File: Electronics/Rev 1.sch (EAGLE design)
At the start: 90 parts, among them Q1 BCV27, Q10 BCV26SOT23, Q11 BCV27, Q12 BCV26SOT23, Q13 BCV27, Q14 BCV26SOT23, Q15 BCV27, Q16 BCV26SOT23, Q17 BCV27, Q18 BCV26SOT23, Q19 BCV27, Q2 BCV26SOT23, Q20 BCV26SOT23, Q21 BCV27, Q22 BCV26SOT23, Q23 BCV27, Q24 BCV26SOT23, Q25 PBSS4360XFPBSS4360XF, Q26 MMBT3904,215MMBT3904,215, Q27 PBSS4360XFPBSS4360XF, Q28 MMBT3904,215MMBT3904,215, Q29 PBSS4360XFPBSS4360XF, Q3 BCV27, Q30 TIP35CTIP35C, Q31 PBSS4360XFPBSS4360XF, Q32 MMBT3904,215MMBT3904,215, Q33 TIP35CTIP35C, Q34 PBSS4360XFPBSS4360XF, Q35 MMBT3904,215MMBT3904,215, Q4 BCV26SOT23, Q5 BCV27, Q6 BCV26SOT23, Q7 BCV27, Q8 BCV26SOT23, Q9 BCV27, U1 LFXP6E-3FN256C, U2 MCP4251, U3 MCP4251, U4 MMA8453QR116QFN

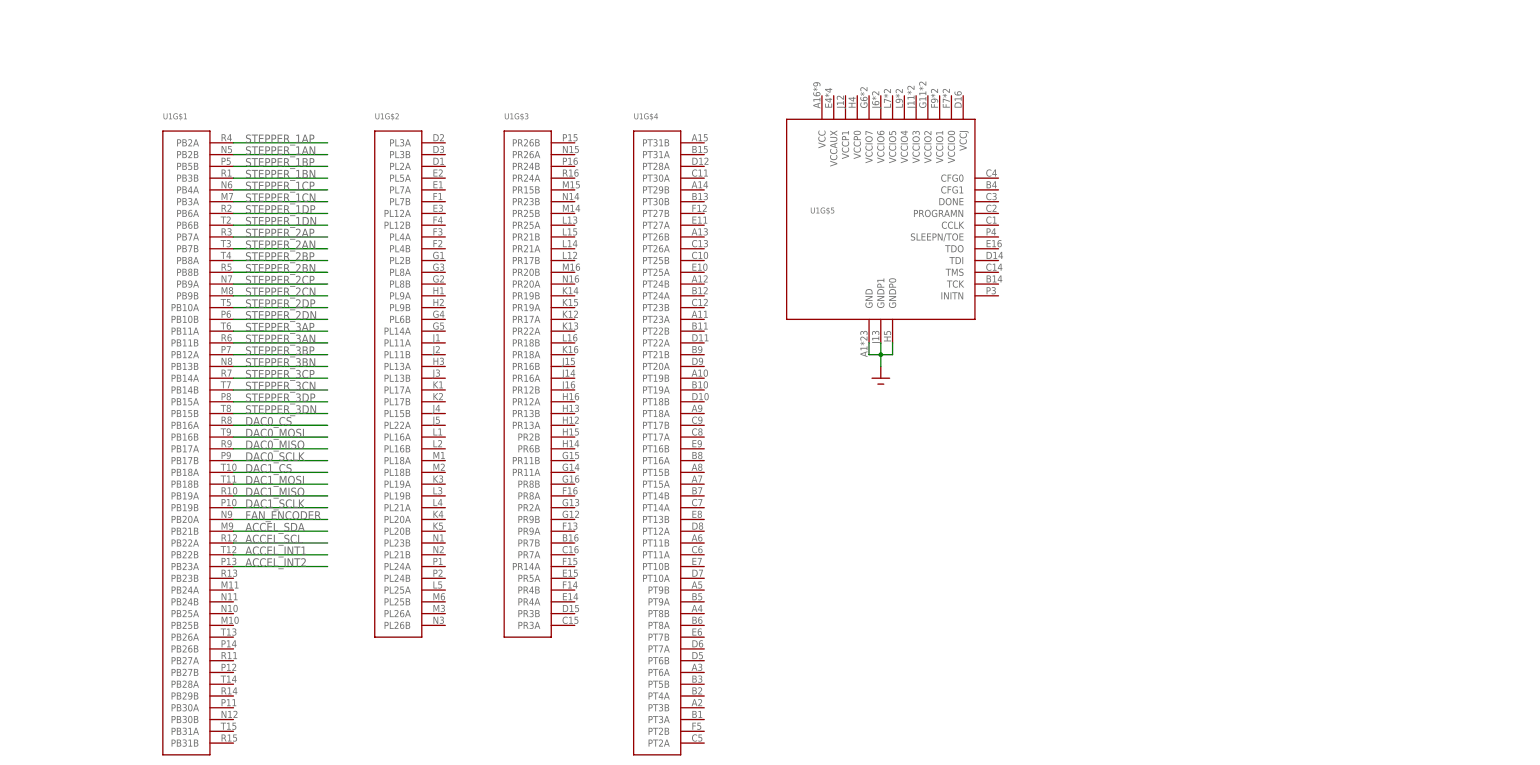
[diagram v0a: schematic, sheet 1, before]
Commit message: Did most of the rest of the schematic
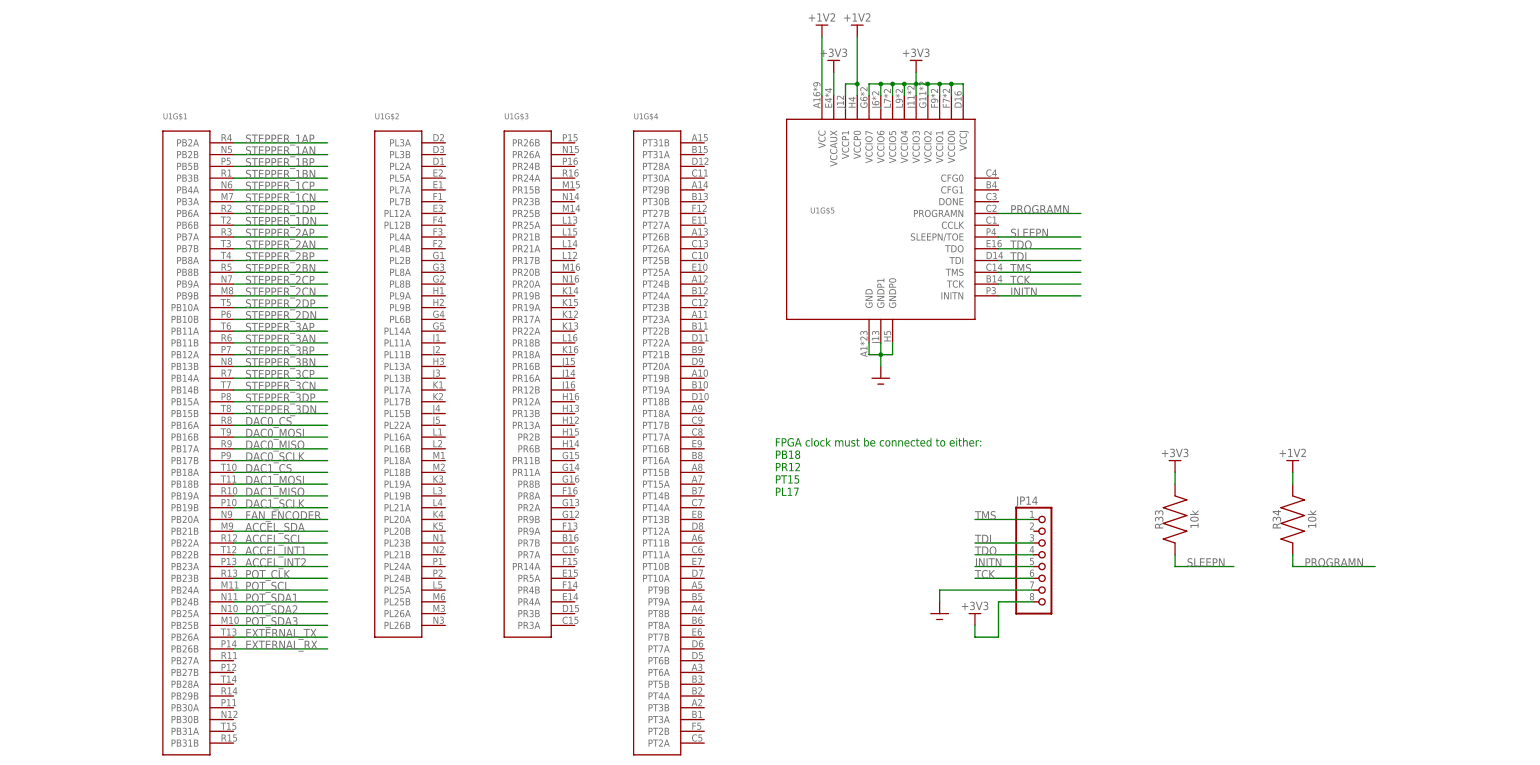
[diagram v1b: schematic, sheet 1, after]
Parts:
- added C27, C28, C29, C30, C31, C32: 0.1uF, fillament-winder:CAPACITOR0805
- added C33: 1uF, fillament-winder:CAPACITOR0805
- added JP11: (no value), fillament-winder:PINHD-1X6
- added JP12, JP13: (no value), fillament-winder:PINHD-1X7
- added JP14: (no value), fillament-winder:PINHD-1X8
- added Q36, Q37, Q38, Q39: MMBT3904,215MMBT3904,215, fillament-winder:MMBT3904,215MMBT3904,215
- added R16, R17, R18: POTENTIOMETER, fillament-winder:POTENTIOMETER
- added R19, R20, R21, R22, R25, R28, R33, R34: 10k, fillament-winder:RESISTOR0805
- added R23, R24, R27: 0R, fillament-winder:RESISTOR0805
- added R26: 1k, fillament-winder:RESISTOR0805
- added U10: RPI, fillament-winder:RPI
- added U5, U6, U7: 74AHC1G66GW,125TSSOP6, fillament-winder:74AHC1G66GW,125TSSOP6
- added U8: MCP3021A1T-E/OTSOT23, fillament-winder:MCP3021A1T-E/OTSOT23
- added U9: MC74HC164BDR2GMC74HC164BDR2G, fillament-winder:MC74HC164BDR2GMC74HC164BDR2G
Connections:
- new net +1V2: R34.P$2, U1G$5.VCC, U1G$5.VCCP0, U1G$5.VCCP1
- new net +5V: C33.P$2, U10.+5V
- new net EXTERNAL_RX: U10.RX, U1G$1.PB26B
- new net EXTERNAL_TX: U10.TX, U1G$1.PB26A
- new net INITN: JP14.5, U1G$5.INITN
- new net N$15: R16.P$1, U5.Y
- new net N$16: R17.P$1, U6.Y
- new net N$19: R18.P$1, U7.Y
- new net N$20: Q36.B, R21.P$2
- new net N$21: R19.P$1, U9.A1
- new net N$22: Q37.B, R22.P$2
- new net N$23: R23.P$1, R24.P$1, U9.QC
- new net N$24: Q38.B, R25.P$2
- new net N$25: Q39.B, R26.P$2
- new net N$27: Q39.E, R27.P$1
- new net POT_ADC: U5.Z, U6.Z, U7.Z, U8.AIN
- new net POT_CLK: JP11.3, JP12.3, JP13.3, U1G$1.PB23B, U9.CLK
- new net POT_RST: R24.P$2, U9.QD, U9.RST
- new net POT_SCL: JP11.4, JP12.4, JP13.4, U1G$1.PB24A, U8.SCL
- new net POT_SDA1: JP12.5, JP13.5, U1G$1.PB24B, U8.SDA
- new net POT_SDA2: JP11.5, JP12.6, JP13.6, U1G$1.PB25A
- new net POT_SDA3: JP11.6, JP12.7, JP13.7, U1G$1.PB25B
- new net POT_SEL_1: R23.P$2, R25.P$1, R27.P$2, U5.E
- new net POT_SEL_2: R21.P$1, R28.P$1, U6.E, U9.QA
- new net POT_SEL_3: R22.P$1, U7.E, U9.QB
- new net POT_SEL_IN: R26.P$1
- new net POT_SHIFT_IN: Q36.C, Q37.C, Q38.C, R20.P$1, U9.A2
- new net PROGRAMN: R34.P$1, U1G$5.PROGRAMN
- new net SLEEPN: R33.P$1, U1G$5.SLEEPN/TOE
- new net TCK: JP14.6, U1G$5.TCK
- new net TDI: JP14.3, U1G$5.TDI
- new net TDO: JP14.4, U1G$5.TDO
- new net TMS: JP14.1, U1G$5.TMS
- net +3V3: now also C27.P$2, C28.P$2, C29.P$2, C30.P$2, C31.P$2, C32.P$2, JP11.1, JP12.1, JP13.1, JP14.8, Q39.C, R19.P$2, R20.P$2, R28.P$2, R33.P$2, U1G$5.VCCAUX, U1G$5.VCCIO0, U1G$5.VCCIO1, U1G$5.VCCIO2, U1G$5.VCCIO3, U1G$5.VCCIO4, U1G$5.VCCIO5, U1G$5.VCCIO6, U1G$5.VCCIO7, U1G$5.VCCJ, U5.VCC, U6.VCC, U7.VCC, U8.VDD, U9.VCC
- net GND: now also C27.P$1, C28.P$1, C29.P$1, C30.P$1, C31.P$1, C32.P$1, C33.P$1, JP11.2, JP12.2, JP13.2, JP14.7, Q36.E, Q37.E, Q38.E, U10.GND, U5.GND, U6.GND, U7.GND, U8.VSS, U9.GND
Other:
- note added: "FPGA clock must be connected to either: PB18 PR12 PT15 PL17"

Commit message: Finished more of the schematic
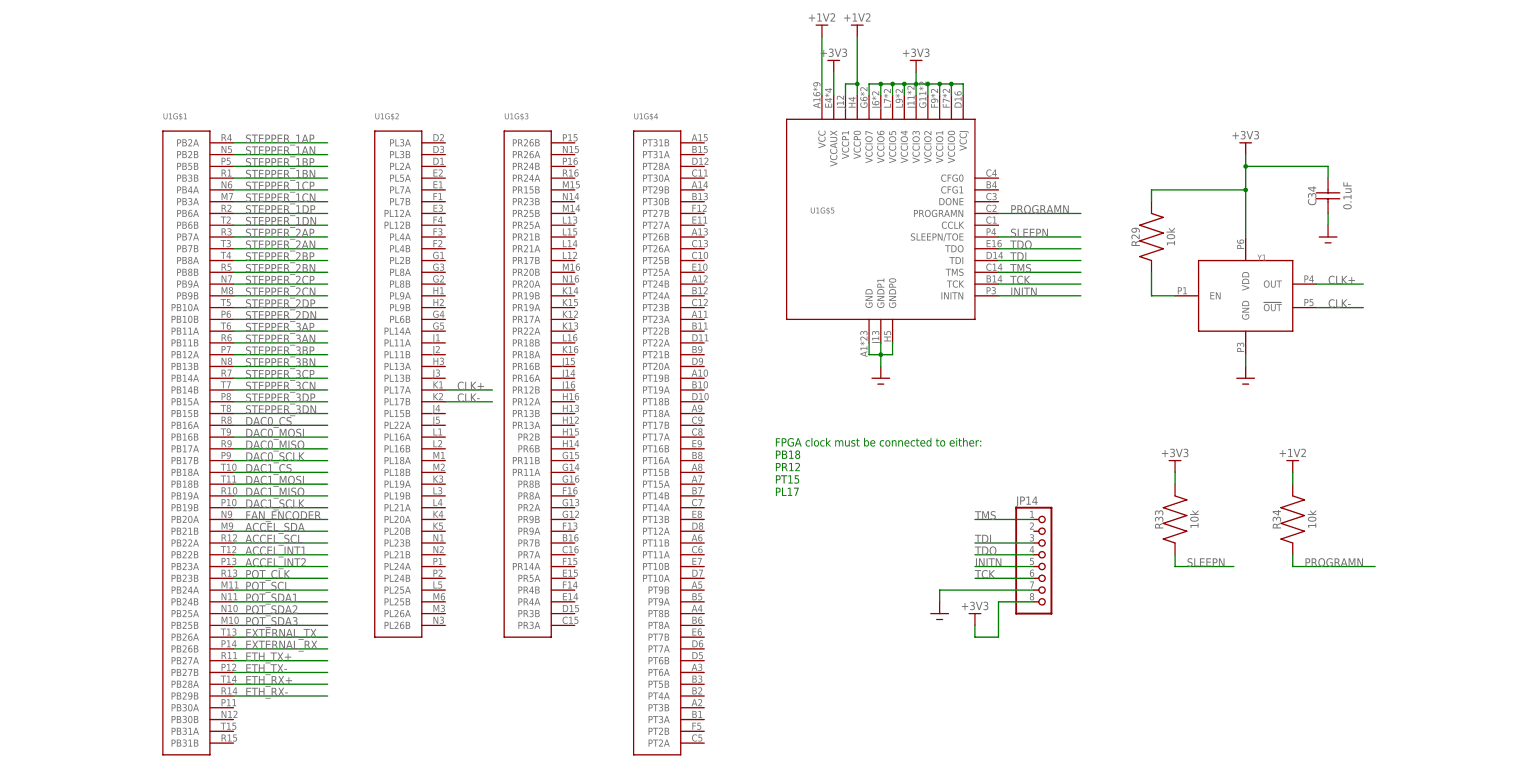
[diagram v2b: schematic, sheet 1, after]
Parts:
- added C34, C35, C36, C37, C38: 0.1uF, fillament-winder:CAPACITOR0805
- added P1: 5-2301994-4, fillament-winder:5-2301994-4
- added R29: 10k, fillament-winder:RESISTOR0805
- added R30, R31, R32, R35: 49.9R, fillament-winder:RESISTOR0805
- added Y1: DSC1122B, fillament-winder:DSC1122B
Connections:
- new net +1V65: C37.P$2, C38.P$2, P1.RCTR, P1.TCTR
- new net CLK+: U1G$2.PL17A, Y1.OUT
- new net CLK-: U1G$2.PL17B, Y1.!OUT
- new net ETH_RX+: P1.RX, R32.P$2, U1G$1.PB28A
- new net ETH_RX-: P1.!RX, R35.P$2, U1G$1.PB29B
- new net ETH_TX+: P1.TX, R30.P$2, U1G$1.PB27A
- new net ETH_TX-: P1.!TX, R31.P$2, U1G$1.PB27B
- new net N$26: C35.P$2, R30.P$1, R31.P$1
- new net N$28: C36.P$2, R32.P$1, R35.P$1
- new net N$29: R29.P$1, Y1.EN
- net +3V3: now also C34.P$2, R29.P$2, Y1.VDD
- net GND: now also C34.P$1, C35.P$1, C36.P$1, C37.P$1, C38.P$1, P1.GND, Y1.GND

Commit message: Added power circuitry
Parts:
- added C39, C40, C41, C42, C43, C44: 1uF, fillament-winder:CAPACITOR0805
- added JP15, JP16, JP17: (no value), fillament-winder:PINHD-1X1
- added JP18: (no value), fillament-winder:PINHD-1X3
- added R36: 2.4k, fillament-winder:RESISTOR0805
- added R37: 7.5k, fillament-winder:RESISTOR0805
- added R38, R39, R40: 0R, fillament-winder:RESISTOR0805
- added U11, U12, U13: 3.3V, fillament-winder:AZ1117E
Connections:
- new net N$31: R36.P$1, R37.P$2, U12.GND
- net +12V: now also JP18.1, R38.P$1, R39.P$1, R40.P$1
- net +1V2: now also C44.P$2, U13.OUT
- net +1V65: now also C42.P$2, R36.P$2, U12.OUT
- net +3V3: now also C40.P$2, C41.P$2, C43.P$2, U11.OUT, U12.IN, U13.IN
- net +5V: now also C39.P$2, JP18.2, U11.IN
- net GND: now also C39.P$1, C40.P$1, C41.P$1, C42.P$1, C43.P$1, C44.P$1, JP18.3, R37.P$1, U11.GND, U13.GND
- net MOTOR_PWR: now also JP17.1, R40.P$2
- net STEPPER_PWR: now also JP15.1, JP16.1, R38.P$2, R39.P$2

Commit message: Cleaned up schematic some
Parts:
- added C45, C46, C47, C49: 0.1uF, fillament-winder:CAPACITOR0805
- added C48: 68nF, fillament-winder:CAPACITOR0805
- added JP19, JP20, JP21, JP22, JP23, JP24, JP25, JP26: (no value), fillament-winder:PINHD-1X2
- added R41: 246k, fillament-winder:RESISTOR0805
- added R42: 1k, fillament-winder:RESISTOR0805
- added R43: 47k, fillament-winder:RESISTOR0805
- added R44: 91k, fillament-winder:RESISTOR0805
- added R45, R46, R47, R48, R49, R50, R51: 4.7k, fillament-winder:RESISTOR0805
- added U14: LT1025CN8PBF, fillament-winder:LT1025CN8PBF
- added U15: LTC1049CS8#PBF, fillament-winder:LTC1049CS8#PBF
- added U16: MCP3021A1T-E/OTSOT23, fillament-winder:MCP3021A1T-E/OTSOT23
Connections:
- new net COMM_1N: JP19.2, U1G$1.PB30B
- new net COMM_1P: JP19.1, U1G$1.PB30A
- new net COMM_2N: JP20.2, U1G$1.PB31B
- new net COMM_2P: JP20.1, U1G$1.PB31A
- new net COMM_3N: JP21.2, U1G$2.PL3B
- new net COMM_3P: JP21.1, U1G$2.PL3A
- new net N$30: C46.P$2, JP24.2, U15.+IN
- new net N$32: C48.P$1, R41.P$1, R42.P$2, U15.-IN
- new net N$33: JP24.1, U14.K
- new net N$34: C48.P$2, R41.P$2, R43.P$2, U15.OUT
- new net N$35: R43.P$1, R44.P$2, U16.AIN
- new net THERMO_SCL: JP25.1, JP26.1, R46.P$1, U16.SCL, U1G$2.PL2A
- new net THERMO_SDA1: JP26.2, R45.P$1, U16.SDA, U1G$2.PL5A
- new net THERMO_SDA2: JP25.2, R47.P$1, U1G$2.PL7A
- net +3V3: now also C49.P$2, R45.P$2, R46.P$2, R47.P$2, R48.P$2, R49.P$2, R50.P$2, R51.P$2, U16.VDD
- net +5V: now also C45.P$2, C47.P$2, U14.VIN, U15.V+
- net GND: now also C45.P$1, C46.P$1, C47.P$1, C49.P$1, R42.P$1, R44.P$1, U14.GND, U14.R-COMMON, U15.V-, U16.VSS
- net HEATER_0: now also JP22.2, JP23.1
- net POT_SCL: now also R51.P$1
- net POT_SDA1: now also R50.P$1
- net POT_SDA2: now also R48.P$1
- net POT_SDA3: now also R49.P$1
- net STEPPER_PWR: now also JP22.1, JP23.2
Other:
- moved on the sheet: U1G$1, U1G$2

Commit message: Started board layout
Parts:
- removed JP13: (no value), fillament-winder:PINHD-1X7
- added D1, D10, D11, D12, D13, D14, D15, D16, D17, D18, D19, D2, D20, D21, D22, D23, D24, D3, D4, D5, D6, D7, D8, D9: M7, fillament-winder:M7
- added U$1: PCB_ACCEL, fillament-winder:PCB_ACCEL
- added U$2: PCB_MAIN, fillament-winder:PCB_MAIN
- added U$3: PCB_POT, fillament-winder:PCB_POT
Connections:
- removed net POT_SEL_IN: R26.P$1
- net +3V3: no longer JP13.1
- net CLK+: now also U1G$2.PL14A; no longer U1G$2.PL17A
- net CLK-: now also U1G$2.PL19B; no longer U1G$2.PL17B
- net COMM_3N: now also U1G$2.PL25A; no longer U1G$2.PL3B
- net COMM_3P: now also U1G$2.PL19A; no longer U1G$2.PL3A
- net GND: now also D10.IN, D12.IN, D14.IN, D16.IN, D18.IN, D2.IN, D20.IN, D22.IN, D24.IN, D4.IN, D6.IN, D8.IN; no longer JP13.2
- net POT_CLK: no longer JP13.3
- net POT_SCL: no longer JP13.4
- net POT_SDA1: no longer JP13.5
- net POT_SDA2: no longer JP13.6
- net POT_SDA3: no longer JP13.7
- net POT_SHIFT_IN: now also R26.P$1
- net STEPPER_1A: now also D1.IN, D2.OUT
- net STEPPER_1AN: now also U1G$2.PL26B; no longer U1G$1.PB2B
- net STEPPER_1AP: now also U1G$2.PL3B; no longer U1G$1.PB2A
- net STEPPER_1B: now also D3.IN, D4.OUT
- net STEPPER_1BN: now also U1G$2.PL24B; no longer U1G$1.PB3B
- net STEPPER_1BP: now also U1G$2.PL2A; no longer U1G$1.PB5B
- net STEPPER_1C: now also D5.IN, D6.OUT
- net STEPPER_1CN: now also U1G$2.PL24A; no longer U1G$1.PB3A
- net STEPPER_1CP: now also U1G$2.PL3A; no longer U1G$1.PB4A
- net STEPPER_1D: now also D7.IN, D8.OUT
- net STEPPER_1DN: now also U1G$2.PL21B; no longer U1G$1.PB6B
- net STEPPER_1DP: now also U1G$2.PL7A; no longer U1G$1.PB6A
- net STEPPER_2A: now also D10.OUT, D9.IN
- net STEPPER_2AN: now also U1G$2.PL23B; no longer U1G$1.PB7B
- net STEPPER_2AP: now also U1G$2.PL5A; no longer U1G$1.PB7A
- net STEPPER_2B: now also D11.IN, D12.OUT
- net STEPPER_2BN: now also U1G$2.PL18B; no longer U1G$1.PB8B
- net STEPPER_2BP: now also U1G$2.PL7B; no longer U1G$1.PB8A
- net STEPPER_2C: now also D13.IN, D14.OUT
- net STEPPER_2CN: now also U1G$2.PL18A; no longer U1G$1.PB9B
- net STEPPER_2CP: now also U1G$2.PL4B; no longer U1G$1.PB9A
- net STEPPER_2D: now also D15.IN, D16.OUT
- net STEPPER_2DN: now also U1G$2.PL16B; no longer U1G$1.PB10B
- net STEPPER_2DP: now also U1G$2.PL2B; no longer U1G$1.PB10A
- net STEPPER_3A: now also D17.IN, D18.OUT
- net STEPPER_3AN: now also U1G$2.PL16A; no longer U1G$1.PB11B
- net STEPPER_3AP: now also U1G$2.PL8B; no longer U1G$1.PB11A
- net STEPPER_3B: now also D19.IN, D20.OUT
- net STEPPER_3BN: now also U1G$2.PL17B; no longer U1G$1.PB13B
- net STEPPER_3BP: now also U1G$2.PL9A; no longer U1G$1.PB12A
- net STEPPER_3C: now also D21.IN, D22.OUT
- net STEPPER_3CN: now also U1G$2.PL17A; no longer U1G$1.PB14B
- net STEPPER_3CP: now also U1G$2.PL9B; no longer U1G$1.PB14A
- net STEPPER_3D: now also D23.IN, D24.OUT
- net STEPPER_3DN: now also U1G$2.PL11B; no longer U1G$1.PB15B
- net STEPPER_3DP: now also U1G$2.PL11A; no longer U1G$1.PB15A
- net STEPPER_PWR: now also D1.OUT, D11.OUT, D13.OUT, D15.OUT, D17.OUT, D19.OUT, D21.OUT, D23.OUT, D3.OUT, D5.OUT, D7.OUT, D9.OUT
- net THERMO_SCL: now also U1G$2.PL13B; no longer U1G$2.PL2A
- net THERMO_SDA1: now also U1G$2.PL20B; no longer U1G$2.PL5A
- net THERMO_SDA2: now also U1G$2.PL21A; no longer U1G$2.PL7A

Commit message: Layed out board
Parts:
- removed JP10: (no value), fillament-winder:PINHD-1X6
- added C50: 0.1uF, fillament-winder:CAPACITOR0805
- added JP13: (no value), fillament-winder:PINHD-1X3
- added U$4: PCB_CARVER, fillament-winder:PCB_CARVER
- R12, R6: value 10k -> 1M
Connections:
- removed net COMM_1N: JP19.2, U1G$1.PB30B
- removed net COMM_1P: JP19.1, U1G$1.PB30A
- removed net COMM_2N: JP20.2, U1G$1.PB31B
- removed net COMM_2P: JP20.1, U1G$1.PB31A
- removed net COMM_3N: JP21.2, U1G$2.PL25A
- removed net COMM_3P: JP21.1, U1G$2.PL19A
- removed net ETH_RX+: P1.RX, R32.P$2, U1G$1.PB28A
- removed net ETH_RX-: P1.!RX, R35.P$2, U1G$1.PB29B
- removed net ETH_TX+: P1.TX, R30.P$2, U1G$1.PB27A
- removed net ETH_TX-: P1.!TX, R31.P$2, U1G$1.PB27B
- new net COMM_1_N: JP19.2, U1G$1.PB11B
- new net COMM_1_P: JP19.1, U1G$1.PB11A
- new net COMM_2_N: JP20.2, U1G$1.PB7B
- new net COMM_2_P: JP20.1, U1G$1.PB7A
- new net COMM_3_N: JP21.2, U1G$1.PB6B
- new net COMM_3_P: JP21.1, U1G$1.PB6A
- new net ETH_RX_N: P1.!RX, R35.P$2, U1G$1.PB31B
- new net ETH_RX_P: P1.RX, R32.P$2, U1G$1.PB31A
- new net ETH_TX_N: P1.!TX, R31.P$2, U1G$1.PB18B
- new net ETH_TX_P: P1.TX, R30.P$2, U1G$1.PB18A
- new net HEATER_PWR: C14.P$2, C15.P$2, C16.P$2, C17.P$2, JP16.1, JP22.1, JP23.2, JP4.1, JP5.1, Q26.C, Q28.C, R39.P$2
- net +12V: now also C50.P$2
- net +3V3: now also JP13.2; no longer JP10.6
- net +5V: now also JP13.1
- net ACCEL_INT1: now also U1G$4.PT26B; no longer JP10.2, U1G$1.PB22B
- net ACCEL_INT2: now also U1G$4.PT24B; no longer JP10.1, U1G$1.PB23A
- net ACCEL_SCL: now also U1G$4.PT29B; no longer JP10.4, U1G$1.PB22A
- net ACCEL_SDA: now also U1G$4.PT31B; no longer JP10.5, U1G$1.PB21B
- net CLK+: now also U1G$3.PR12A; no longer U1G$2.PL14A
- net CLK-: now also U1G$3.PR12B; no longer U1G$2.PL19B
- net DAC0_CS: now also U1G$4.PT27B; no longer U1G$1.PB16A
- net DAC0_MISO: now also U1G$4.PT28A; no longer U1G$1.PB17A
- net DAC0_MOSI: now also U1G$4.PT31A; no longer U1G$1.PB16B
- net DAC0_SCLK: now also U1G$4.PT26A; no longer U1G$1.PB17B
- net DAC1_CS: now also U1G$4.PT9A; no longer U1G$1.PB18A
- net DAC1_MISO: now also U1G$4.PT9B; no longer U1G$1.PB19A
- net DAC1_MOSI: now also U1G$4.PT8A; no longer U1G$1.PB18B
- net DAC1_SCLK: now also U1G$4.PT11B; no longer U1G$1.PB19B
- net EXTERNAL_RX: now also U1G$1.PB15A; no longer U1G$1.PB26B
- net EXTERNAL_TX: now also U1G$1.PB9A; no longer U1G$1.PB26A
- net FAN_ENCODER: now also U1G$4.PT8B; no longer U1G$1.PB20A
- net GND: now also C50.P$1, JP13.3; no longer JP10.3
- net POT_CLK: now also U1G$4.PT6A; no longer U1G$1.PB23B
- net POT_SCL: now also U1G$4.PT3B; no longer U1G$1.PB24A
- net POT_SDA1: now also U1G$4.PT10A; no longer U1G$1.PB24B
- net POT_SDA2: now also U1G$4.PT7A; no longer U1G$1.PB25A
- net POT_SDA3: now also U1G$4.PT6B; no longer U1G$1.PB25B
- net STEPPER_PWR: no longer C14.P$2, C15.P$2, C16.P$2, C17.P$2, JP16.1, JP22.1, JP23.2, JP4.1, JP5.1, Q26.C, Q28.C, R39.P$2
- net THERMO_SCL: now also U1G$4.PT14B; no longer U1G$2.PL13B
- net THERMO_SDA1: now also U1G$4.PT15B; no longer U1G$2.PL20B
- net THERMO_SDA2: now also U1G$4.PT15A; no longer U1G$2.PL21A
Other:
- moved on the sheet: U1G$1, U1G$2, U1G$3, U1G$4
